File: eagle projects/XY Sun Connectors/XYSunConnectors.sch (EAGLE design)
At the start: 2 parts, among them J1 FPC_HIROSE_FH19C-6S-0.5SH(10)

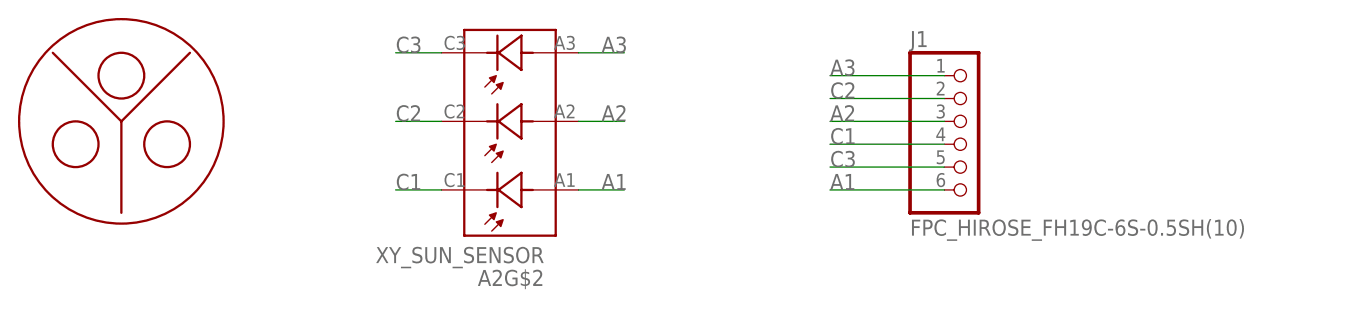
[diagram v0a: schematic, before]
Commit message: Updated XY Sun Sensor Board
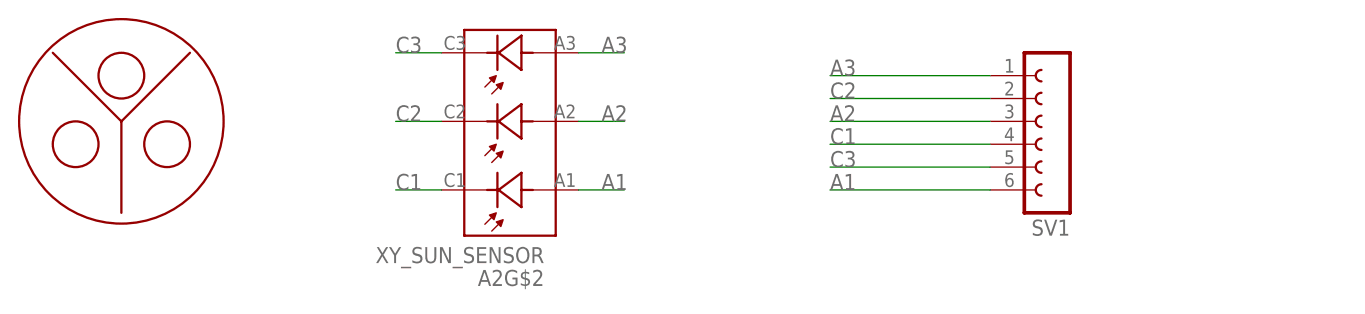
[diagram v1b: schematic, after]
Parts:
- removed J1: FPC_HIROSE_FH19C-6S-0.5SH(10), my_library:FPC_HIROSE_FH19C-6S-0.5SH(10)
- added SV1: (no value), con-lsta:FE06-1
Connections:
- net A1: now also SV1.6; no longer J1.6
- net A2: now also SV1.3; no longer J1.3
- net A3: now also SV1.1; no longer J1.1
- net C1: now also SV1.4; no longer J1.4
- net C2: now also SV1.2; no longer J1.2
- net C3: now also SV1.5; no longer J1.5
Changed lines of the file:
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@@
 <parts>
 <part name="FRAME1" library="my_library" library_urn="urn:adsk.eagle:library:22876504" deviceset="TITLE_BLOCK_LETTER" device=""/>
-<part name="J1" library="my_library" library_urn="urn:adsk.eagle:library:22876504" deviceset="FPC_HIROSE_FH19C-6S-0.5SH(10)" device=""/>
 <part name="A2" library="my_library" library_urn="urn:adsk.eagle:library:22876504" deviceset="XY_SUN_SENSOR" device=""/>
+<part name="SV1" library="con-lsta" library_urn="urn:adsk.eagle:library:161" deviceset="FE06-1" device="" package3d_urn="urn:adsk.eagle:package:8191/1"/>
 </parts>
 <sheets>
@@
 <attribute name="DRAWING_NAME" x="190.5" y="19.05" size="2.54" layer="94"/>
 </instance>
-<instance part="J1" gate="G$1" x="177.8" y="111.76" smashed="yes">
-<attribute name="NAME" x="171.45" y="122.555" size="1.778" layer="95"/>
-<attribute name="VALUE" x="171.45" y="101.6" size="1.778" layer="96"/>
-</instance>
 <instance part="A2" gate="G$2" x="127" y="114.3" smashed="yes" rot="R180">
 <attribute name="NAME" x="130.81" y="97.79" size="1.778" layer="95" rot="R180"/>
@@
 </instance>
 <instance part="A2" gate="G$1" x="68.58" y="121.92" smashed="yes"/>
+<instance part="SV1" gate="G$1" x="187.96" y="114.3" smashed="yes" rot="R180">
+<attribute name="VALUE" x="189.23" y="124.46" size="1.778" layer="96" rot="R180"/>
+<attribute name="NAME" x="189.23" y="103.378" size="1.778" layer="95" rot="R180"/>
+</instance>
 </instances>
 <busses>
@@
 <net name="A3" class="0">
 <segment>
-<pinref part="J1" gate="G$1" pin="1"/>
-<wire x1="175.26" y1="119.38" x2="162.56" y2="119.38" width="0.1524" layer="91"/>
+<wire x1="180.34" y1="119.38" x2="162.56" y2="119.38" width="0.1524" layer="91"/>
 <label x="162.56" y="119.38" size="1.778" layer="95"/>
+<pinref part="SV1" gate="G$1" pin="1"/>
 </segment>
 <segment>
@@
 <net name="C3" class="0">
 <segment>
-<pinref part="J1" gate="G$1" pin="5"/>
-<wire x1="175.26" y1="109.22" x2="162.56" y2="109.22" width="0.1524" layer="91"/>
+<wire x1="180.34" y1="109.22" x2="162.56" y2="109.22" width="0.1524" layer="91"/>
 <label x="162.56" y="109.22" size="1.778" layer="95"/>
+<pinref part="SV1" gate="G$1" pin="5"/>
 </segment>
 <segment>
@@
 <net name="C2" class="0">
 <segment>
-<pinref part="J1" gate="G$1" pin="2"/>
-<wire x1="162.56" y1="116.84" x2="175.26" y2="116.84" width="0.1524" layer="91"/>
+<wire x1="162.56" y1="116.84" x2="180.34" y2="116.84" width="0.1524" layer="91"/>
 <label x="162.56" y="116.84" size="1.778" layer="95"/>
+<pinref part="SV1" gate="G$1" pin="2"/>
 </segment>
 <segment>
@@
 <net name="C1" class="0">
 <segment>
-<pinref part="J1" gate="G$1" pin="4"/>
-<wire x1="175.26" y1="111.76" x2="162.56" y2="111.76" width="0.1524" layer="91"/>
+<wire x1="180.34" y1="111.76" x2="162.56" y2="111.76" width="0.1524" layer="91"/>
 <label x="162.56" y="111.76" size="1.778" layer="95"/>
+<pinref part="SV1" gate="G$1" pin="4"/>
 </segment>
 <segment>
@@
 <net name="A2" class="0">
 <segment>
-<pinref part="J1" gate="G$1" pin="3"/>
-<wire x1="175.26" y1="114.3" x2="162.56" y2="114.3" width="0.1524" layer="91"/>
+<wire x1="180.34" y1="114.3" x2="162.56" y2="114.3" width="0.1524" layer="91"/>
 <label x="162.56" y="114.3" size="1.778" layer="95"/>
+<pinref part="SV1" gate="G$1" pin="3"/>
 </segment>
 <segment>
@@
 <net name="A1" class="0">
 <segment>
-<pinref part="J1" gate="G$1" pin="6"/>
-<wire x1="175.26" y1="106.68" x2="162.56" y2="106.68" width="0.1524" layer="91"/>
+<wire x1="180.34" y1="106.68" x2="162.56" y2="106.68" width="0.1524" layer="91"/>
 <label x="162.56" y="106.68" size="1.778" layer="95"/>
+<pinref part="SV1" gate="G$1" pin="6"/>
 </segment>
 <segment>
@@
 will not be understood (or retained) with this version.
 </note>
+<note version="8.3" severity="warning">
+Since Version 8.3, EAGLE supports the association of 3D packages
+with devices in libraries, schematics, and board files. Those 3D
+packages will not be understood (or retained) with this version.
+</note>
 </compatibility>

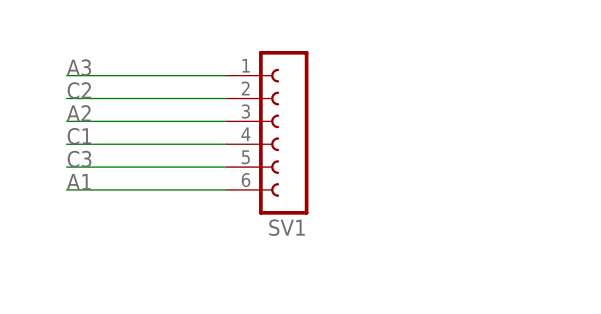
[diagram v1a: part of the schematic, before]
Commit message: Added proper connectors on XY Sun Connectors
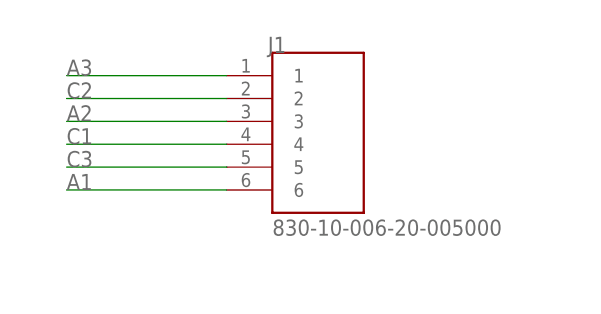
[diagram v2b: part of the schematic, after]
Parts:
- removed SV1: (no value), con-lsta:FE06-1
- added J1: 830-10-006-20-005000, 830-10-006-20-005000:830-10-006-20-005000
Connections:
- net A1: now also J1.6; no longer SV1.6
- net A2: now also J1.3; no longer SV1.3
- net A3: now also J1.1; no longer SV1.1
- net C1: now also J1.4; no longer SV1.4
- net C2: now also J1.2; no longer SV1.2
- net C3: now also J1.5; no longer SV1.5
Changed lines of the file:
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@@
 <parts>
 <part name="FRAME1" library="my_library" library_urn="urn:adsk.eagle:library:22876504" deviceset="TITLE_BLOCK_LETTER" device=""/>
-<part name="A2" library="my_library" library_urn="urn:adsk.eagle:library:22876504" deviceset="XY_SUN_SENSOR" device=""/>
-<part name="SV1" library="con-lsta" library_urn="urn:adsk.eagle:library:161" deviceset="FE06-1" device="" package3d_urn="urn:adsk.eagle:package:8191/1"/>
+<part name="A2" library="my_library" library_urn="urn:adsk.eagle:library:22876504" deviceset="XY_SUN_SENSOR" device="" override_package3d_urn="urn:adsk.eagle:package:31634060/3" override_package_urn="urn:adsk.eagle:footprint:31634061/1"/>
+<part name="J1" library="830-10-006-20-005000" deviceset="830-10-006-20-005000" device="" override_package3d_urn="urn:adsk.eagle:package:31634800/3" override_package_urn="urn:adsk.eagle:footprint:31634826/1"/>
 </parts>
 <sheets>
@@
 </instance>
 <instance part="A2" gate="G$1" x="68.58" y="121.92" smashed="yes"/>
-<instance part="SV1" gate="G$1" x="187.96" y="114.3" smashed="yes" rot="R180">
-<attribute name="VALUE" x="189.23" y="124.46" size="1.778" layer="96" rot="R180"/>
-<attribute name="NAME" x="189.23" y="103.378" size="1.778" layer="95" rot="R180"/>
+<instance part="J1" gate="G$1" x="190.5" y="114.3" smashed="yes">
+<attribute name="NAME" x="184.92" y="121.92" size="1.778" layer="95"/>
+<attribute name="VALUE" x="185.42" y="101.6" size="1.778" layer="96"/>
 </instance>
 </instances>
@@
 <wire x1="180.34" y1="119.38" x2="162.56" y2="119.38" width="0.1524" layer="91"/>
 <label x="162.56" y="119.38" size="1.778" layer="95"/>
-<pinref part="SV1" gate="G$1" pin="1"/>
+<pinref part="J1" gate="G$1" pin="1"/>
 </segment>
 <segment>
@@
 <wire x1="180.34" y1="109.22" x2="162.56" y2="109.22" width="0.1524" layer="91"/>
 <label x="162.56" y="109.22" size="1.778" layer="95"/>
-<pinref part="SV1" gate="G$1" pin="5"/>
+<pinref part="J1" gate="G$1" pin="5"/>
 </segment>
 <segment>
@@
 <wire x1="162.56" y1="116.84" x2="180.34" y2="116.84" width="0.1524" layer="91"/>
 <label x="162.56" y="116.84" size="1.778" layer="95"/>
-<pinref part="SV1" gate="G$1" pin="2"/>
+<pinref part="J1" gate="G$1" pin="2"/>
 </segment>
 <segment>
@@
 <wire x1="180.34" y1="111.76" x2="162.56" y2="111.76" width="0.1524" layer="91"/>
 <label x="162.56" y="111.76" size="1.778" layer="95"/>
-<pinref part="SV1" gate="G$1" pin="4"/>
+<pinref part="J1" gate="G$1" pin="4"/>
 </segment>
 <segment>
@@
 <wire x1="180.34" y1="114.3" x2="162.56" y2="114.3" width="0.1524" layer="91"/>
 <label x="162.56" y="114.3" size="1.778" layer="95"/>
-<pinref part="SV1" gate="G$1" pin="3"/>
+<pinref part="J1" gate="G$1" pin="3"/>
 </segment>
 <segment>
@@
 <wire x1="180.34" y1="106.68" x2="162.56" y2="106.68" width="0.1524" layer="91"/>
 <label x="162.56" y="106.68" size="1.778" layer="95"/>
-<pinref part="SV1" gate="G$1" pin="6"/>
+<pinref part="J1" gate="G$1" pin="6"/>
 </segment>
 <segment>
@@
 packages will not be understood (or retained) with this version.
 </note>
+<note version="9.4" severity="warning">
+Since Version 9.4, EAGLE supports the overriding of 3D packages
+in schematics and board files. Those overridden 3d packages
+will not be understood (or retained) with this version.
+</note>
 </compatibility>
